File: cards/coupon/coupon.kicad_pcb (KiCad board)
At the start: 2 copper layers, 100 x 100 mm, 65 parts, among them J1 IN N1 N2 N3, J2 BUS, Q1 2N7000, Q10 2N7000, Q11 2N7000, Q12 2N7000, Q13 2N7000, Q14 2N7000, Q15 2N7000, Q16 2N7000, Q17 2N7000, Q18 2N7000, Q19 2N7000, Q2 2N7000, Q20 2N7000, Q21 2N7000, Q22 2N7000, Q23 2N7000, Q24 2N7000, Q25 2N7000, Q26 2N7000, Q3 2N7000, Q4 2N7000, Q5 2N7000, Q6 2N7000, Q7 2N7000, Q8 2N7000, Q9 2N7000

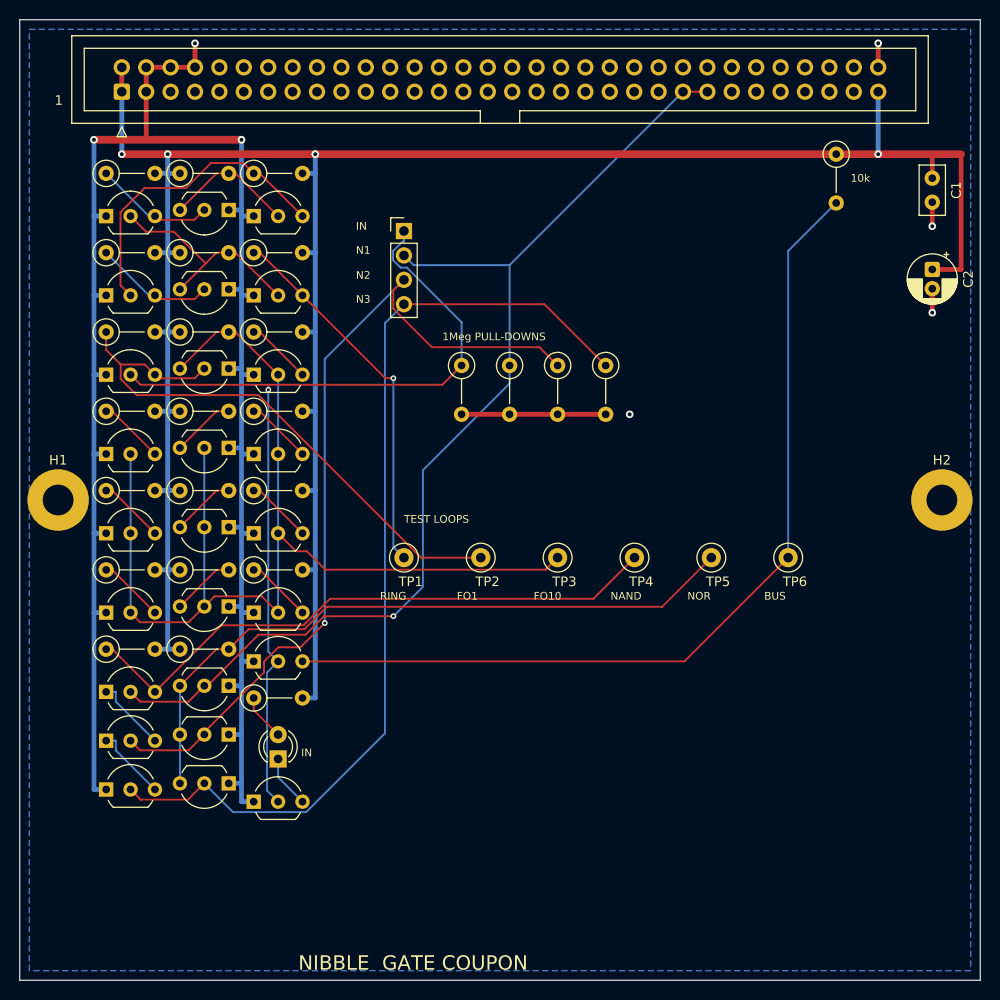
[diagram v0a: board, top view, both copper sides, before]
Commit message: Coupon respun with every cell on it (D056): the bench's expected readings from its own netlist
The coupon is what proves the simulations right before the second order, and
the old one measured only the inverter. It now carries, each with a test
loop: the 5-inverter ring (a buffered loop and a raw one on the ring node),
fan-out 1 and 10, NAND3 and NOR3, the bus driver against 10k, the clock
card's oscillator (its Schmitt pair and 100k + 47 nF, the same parts drawn
on the sheet), a master-slave flip-flop wired as a toggle with the
asynchronous reset the counters and the sequencer use, the D053 line
driver (1k inverter, 100 ohm, diode, 10k pull-down; 3.3 nF clipped on at
the bench), a diode-connected transistor on 4.7k that reads its own
threshold, and a program row (3.3k, 1N4148, 220k). Inputs IN N1 N2 N3 RST
on a 6-pin header with 1 Meg pull-downs, power on a 2-pin header for the
bench supply, fifteen loops. 57 transistors on six tile columns of one
100 x 100 card; ERC 0, one freerouting pass, DRC 0 errors (one dangling
trunk end), 0 open under JLCPCB's minimum rules too.

sim/tb_coupon.py simulates the routed card's kicad export (or the gate list
plus the sheet parts, which agree at every uniform corner) at TYP, LO, HI
and MIX seeds 1..3, a x10 probe on every loop, and writes the bands the
bench must land in: sim/results/coupon_expected.md. Ring 5.9 to 23.6 us
(14.6 typical), fan-out-1 rise 10 to 12 us, fan-out-10 rise 67 to 77 us,
stacks under 2 mV, Schmitt hysteresis 0.4 V about the threshold,
oscillator 1.64 to 2.55 ms, Q at half that with one edge per clock edge,
DRV 4.0 V high, 6.6 us up and 49 us down into 3.3 nF, VTO 0.88 to 3.02 V,
ROM 4.52 V, 5 to 8 mA with IN low and 11 to 14 mA with IN high.

Two things the testbench found before the copper did: with low-threshold
transistors the ring swings only to 1.6 to 3 V and a high-threshold buffer
never switches (the buffered loop was blind at two MIX seeds; hence the
raw RING0 loop), and while RST holds the flip-f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
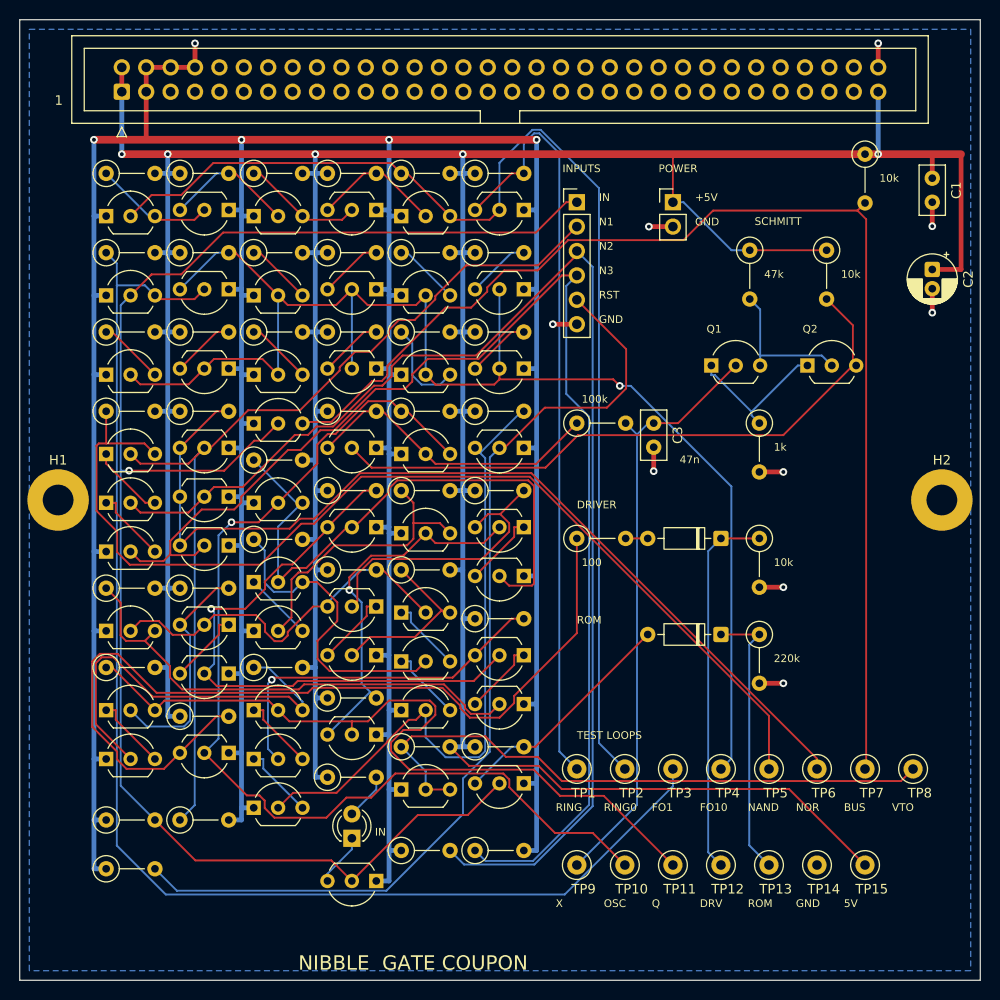
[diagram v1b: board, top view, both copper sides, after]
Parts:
- added C3: 47n, C_Disc_D5.0mm_W2.5mm_P2.50mm, F.Cu at (66.0, 42.0)
- added D2: 1N4148, D_DO-35_SOD27_P7.62mm_Horizontal, F.Cu at (73.0, 54.0)
- added D3: 1N4148, D_DO-35_SOD27_P7.62mm_Horizontal, F.Cu at (73.0, 64.0)
- added J3: BUS, IDC-Header_2x32_P2.54mm_Vertical, F.Cu at (10.6, 7.50)
- added Q27: 2N7000, TO-92_Inline_Wide, F.Cu at (39.7, 45.2)
- added Q28: 2N7000, TO-92_Inline_Wide, F.Cu at (52.5, 44.6)
- added Q29: 2N7000, TO-92_Inline_Wide, F.Cu at (24.4, 50.3)
- added Q30: 2N7000, TO-92_Inline_Wide, F.Cu at (37.1, 52.8)
- added Q31: 2N7000, TO-92_Inline_Wide, F.Cu at (39.7, 53.5)
- added Q32: 2N7000, TO-92_Inline_Wide, F.Cu at (52.5, 52.8)
- added Q33: 2N7000, TO-92_Inline_Wide, F.Cu at (52.5, 57.9)
- added Q34: 2N7000, TO-92_Inline_Wide, F.Cu at (24.4, 58.5)
- added Q35: 2N7000, TO-92_Inline_Wide, F.Cu at (24.4, 63.6)
- added Q36: 2N7000, TO-92_Inline_Wide, F.Cu at (37.1, 61.1)
- added Q37: 2N7000, TO-92_Inline_Wide, F.Cu at (37.1, 66.2)
- added Q38: 2N7000, TO-92_Inline_Wide, F.Cu at (39.7, 61.7)
- added Q39: 2N7000, TO-92_Inline_Wide, F.Cu at (39.7, 66.8)
- added Q40: 2N7000, TO-92_Inline_Wide, F.Cu at (39.7, 71.9)
- added Q41: 2N7000, TO-92_Inline_Wide, F.Cu at (9.00, 63.6)
- added Q42: 2N7000, TO-92_Inline_Wide, F.Cu at (21.8, 63.0)
- added Q43: 2N7000, TO-92_Inline_Wide, F.Cu at (21.8, 68.1)
- added Q44: 2N7000, TO-92_Inline_Wide, F.Cu at (52.5, 66.2)
- added Q45: 2N7000, TO-92_Inline_Wide, F.Cu at (52.5, 71.2)
- added Q46: 2N7000, TO-92_Inline_Wide, F.Cu at (9.00, 71.9)
- added Q47: 2N7000, TO-92_Inline_Wide, F.Cu at (9.00, 77.0)
- added Q48: 2N7000, TO-92_Inline_Wide, F.Cu at (24.4, 71.9)
- added Q49: 2N7000, TO-92_Inline_Wide, F.Cu at (24.4, 77.0)
- added Q50: 2N7000, TO-92_Inline_Wide, F.Cu at (24.4, 82.0)
- added Q51: 2N7000, TO-92_Inline_Wide, F.Cu at (37.1, 74.4)
- added Q52: 2N7000, TO-92_Inline_Wide, F.Cu at (21.8, 76.3)
- added Q53: 2N7000, TO-92_Inline_Wide, F.Cu at (39.7, 80.1)
- added Q54: 2N7000, TO-92_Inline_Wide, F.Cu at (52.5, 79.5)
- added Q55: 2N7000, TO-92_Inline_Wide, F.Cu at (37.1, 89.7)
- added Q56: 2N7000, TO-92_Inline_Wide, F.Cu at (72.0, 36.0)
- added Q57: 2N7000, TO-92_Inline_Wide, F.Cu at (82.0, 36.0)
- added R27: 47k, R_Axial_DIN0207_L6.3mm_D2.5mm_P5.08mm_Vertical, F.Cu at (39.7, 49.0)
- added R28: 47k, R_Axial_DIN0207_L6.3mm_D2.5mm_P5.08mm_Vertical, F.Cu at (47.4, 49.0)
- added R29: 47k, R_Axial_DIN0207_L6.3mm_D2.5mm_P5.08mm_Vertical, F.Cu at (24.4, 54.1)
- added R30: 47k, R_Axial_DIN0207_L6.3mm_D2.5mm_P5.08mm_Vertical, F.Cu at (32.0, 57.3)
- added R31: 47k, R_Axial_DIN0207_L6.3mm_D2.5mm_P5.08mm_Vertical, F.Cu at (39.7, 57.3)
- added R32: 47k, R_Axial_DIN0207_L6.3mm_D2.5mm_P5.08mm_Vertical, F.Cu at (9.00, 59.2)
- added R33: 47k, R_Axial_DIN0207_L6.3mm_D2.5mm_P5.08mm_Vertical, F.Cu at (16.7, 59.2)
- added R34: 47k, R_Axial_DIN0207_L6.3mm_D2.5mm_P5.08mm_Vertical, F.Cu at (47.4, 62.4)
- added R35: 47k, R_Axial_DIN0207_L6.3mm_D2.5mm_P5.08mm_Vertical, F.Cu at (9.00, 67.4)
- added R36: 47k, R_Axial_DIN0207_L6.3mm_D2.5mm_P5.08mm_Vertical, F.Cu at (24.4, 67.4)
- added R37: 47k, R_Axial_DIN0207_L6.3mm_D2.5mm_P5.08mm_Vertical, F.Cu at (32.0, 70.6)
- added R38: 1k, R_Axial_DIN0207_L6.3mm_D2.5mm_P5.08mm_Vertical, F.Cu at (16.7, 72.5)
- added R39: 4.7k, R_Axial_DIN0207_L6.3mm_D2.5mm_P5.08mm_Vertical, F.Cu at (39.7, 75.7)
- added R40: 3.3k, R_Axial_DIN0207_L6.3mm_D2.5mm_P5.08mm_Vertical, F.Cu at (47.4, 75.7)
- added R41: 1k, R_Axial_DIN0207_L6.3mm_D2.5mm_P5.08mm_Vertical, F.Cu at (32.0, 78.9)
- added R42: 1Meg, R_Axial_DIN0207_L6.3mm_D2.5mm_P5.08mm_Vertical, F.Cu at (9.00, 83.3)
- added R43: 1Meg, R_Axial_DIN0207_L6.3mm_D2.5mm_P5.08mm_Vertical, F.Cu at (16.7, 83.3)
- added R44: 1Meg, R_Axial_DIN0207_L6.3mm_D2.5mm_P5.08mm_Vertical, F.Cu at (39.7, 86.5)
- added R45: 1Meg, R_Axial_DIN0207_L6.3mm_D2.5mm_P5.08mm_Vertical, F.Cu at (47.4, 86.5)
- added R46: 1Meg, R_Axial_DIN0207_L6.3mm_D2.5mm_P5.08mm_Vertical, F.Cu at (9.00, 88.4)
- added R47: 47k, R_Axial_DIN0207_L6.3mm_D2.5mm_P5.08mm_Vertical, F.Cu at (76.0, 24.0)
- added R48: 10k, R_Axial_DIN0207_L6.3mm_D2.5mm_P5.08mm_Vertical, F.Cu at (84.0, 24.0)
- added R49: 1k, R_Axial_DIN0207_L6.3mm_D2.5mm_P5.08mm_Vertical, F.Cu at (77.0, 42.0)
- added R50: 100k, R_Axial_DIN0207_L6.3mm_D2.5mm_P5.08mm_Vertical, F.Cu at (58.0, 42.0)
- added R51: 100, R_Axial_DIN0207_L6.3mm_D2.5mm_P5.08mm_Vertical, F.Cu at (58.0, 54.0)
- added R52: 10k, R_Axial_DIN0207_L6.3mm_D2.5mm_P5.08mm_Vertical, F.Cu at (77.0, 54.0)
- added R53: 220k, R_Axial_DIN0207_L6.3mm_D2.5mm_P5.08mm_Vertical, F.Cu at (77.0, 64.0)
- added TP10: TP_OSC, TestPoint_Loop_D2.50mm_Drill1.0mm, F.Cu at (63.0, 88.0)
- added TP11: TP_Q, TestPoint_Loop_D2.50mm_Drill1.0mm, F.Cu at (68.0, 88.0)
- added TP12: TP_DRV, TestPoint_Loop_D2.50mm_Drill1.0mm, F.Cu at (73.0, 88.0)
- added TP13: TP_ROM, TestPoint_Loop_D2.50mm_Drill1.0mm, F.Cu at (78.0, 88.0)
- added TP14: GND, TestPoint_Loop_D2.50mm_Drill1.0mm, F.Cu at (83.0, 88.0)
- added TP15: +5V, TestPoint_Loop_D2.50mm_Drill1.0mm, F.Cu at (88.0, 88.0)
- added TP7: TP_BUS, TestPoint_Loop_D2.50mm_Drill1.0mm, F.Cu at (88.0, 78.0)
- added TP8: TP_VTO, TestPoint_Loop_D2.50mm_Drill1.0mm, F.Cu at (93.0, 78.0)
- added TP9: X, TestPoint_Loop_D2.50mm_Drill1.0mm, F.Cu at (58.0, 88.0)
- J1: value IN N1 N2 N3 -> IN N1 N2 N3 RST GND; footprint PinHeader_1x04_P2.54mm_Vertical -> PinHeader_1x06_P2.54mm_Vertical
- J2: value BUS -> +5V GND; footprint IDC-Header_2x32_P2.54mm_Vertical -> PinHeader_1x02_P2.54mm_Vertical
- R1: value 1Meg -> 10k
- R2, R3, R4: value 1Meg -> 47k
- R22: value 47k -> 4.7k
- R26: value 1k -> 47k
- R5: value 10k -> 47k
- TP2: value TP_FO1 -> RING0
- TP3: value TP_FO10 -> TP_FO1
- TP4: value TP_NAND -> TP_FO10
- TP5: value TP_NOR -> TP_NAND
- TP6: value TP_BUS -> TP_NOR
- moved J2 58.5 mm to (68.0, 19.0), turned to 0 degrees
- moved R5 53.0 mm to (32.0, 16.0), turned to 0 degrees
- moved R1 47.4 mm to (88.0, 14.0)
- moved R2 46.5 mm to (9.00, 16.0), turned to 0 degrees
- moved R24 45.7 mm to (47.4, 40.8)
- moved R3 44.1 mm to (16.7, 16.0), turned to 0 degrees
- moved R4 41.7 mm to (24.4, 16.0), turned to 0 degrees
- moved Q26 39.0 mm to (37.1, 44.6), turned to 180 degrees
- moved Q16 37.9 mm to (37.1, 36.3), turned to 180 degrees
- moved Q18 37.9 mm to (52.5, 36.3), turned to 180 degrees
- moved R18 34.9 mm to (39.7, 32.5)
- moved R19 34.9 mm to (47.4, 32.5)
- moved Q10 32.9 mm to (37.1, 28.1), turned to 180 degrees
- moved Q12 32.9 mm to (52.5, 28.1), turned to 180 degrees
- moved R12 31.8 mm to (39.7, 24.3)
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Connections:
- J2 pad 2: +5V -> GND
- Q26 pad 2: IN -> VD2
- Q26 pad 3: Net-(D1-K) -> SA
- R1 pad 1: IN -> +5V
- R1 pad 2: GND -> TP_BUS
- R10 pad 1: +5V -> LOAD0
- R10 pad 2: RING0 -> +5V
- R11 pad 1: TP_RING -> +5V
- R11 pad 2: +5V -> LOAD1
- R12 pad 1: TP_FO1 -> LOAD2
- R13 pad 2: TP_FO10 -> LOAD3
- R14 pad 1: LOAD0 -> LOAD4
- R15 pad 1: LOAD1 -> +5V
- R15 pad 2: +5V -> LOAD5
- R16 pad 1: +5V -> LOAD6
- R16 pad 2: LOAD2 -> +5V
- R17 pad 1: LOAD3 -> +5V
- R17 pad 2: +5V -> LOAD7
- R18 pad 1: LOAD4 -> LOAD8
- R19 pad 2: LOAD5 -> LOAD9
- R2 pad 1: N1 -> RING1
- R2 pad 2: GND -> +5V
- R20 pad 1: LOAD6 -> TP_NAND
- R21 pad 1: LOAD7 -> +5V
- R21 pad 2: +5V -> TP_NOR
- R22 pad 2: LOAD8 -> SA
- R23 pad 1: LOAD9 -> TP_OSC
- R24 pad 1: TP_NAND -> +5V
- R24 pad 2: +5V -> RSTN
- R25 pad 1: +5V -> TP_Q_ckn
- R25 pad 2: TP_NOR -> +5V
- R26 pad 1: Net-(D1-A) -> +5V
- R26 pad 2: +5V -> TP_Q_ckb
- R3 pad 1: N2 -> +5V
- R3 pad 2: GND -> RING2
- R4 pad 1: N3 -> RING3
- R4 pad 2: GND -> +5V
- R5 pad 2: TP_BUS -> RING4
- R6 pad 1: RING1 -> RING0
- R7 pad 2: RING2 -> TP_RING
- R8 pad 1: RING3 -> TP_FO1
- R9 pad 1: RING4 -> +5V
- R9 pad 2: +5V -> TP_FO10
- TP2 pad 1: TP_FO1 -> RING0
- TP3 pad 1: TP_FO10 -> TP_FO1
- TP4 pad 1: TP_NAND -> TP_FO10
- TP5 pad 1: TP_NOR -> TP_NAND
- TP6 pad 1: TP_BUS -> TP_NOR
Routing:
- net GND: track 220.5 -> 444.0 mm, vias 7 -> 14
- net +5V: track 256.1 -> 428.9 mm, vias 4 -> 5
- net TP_OSC: track 0.00 -> 109.9 mm, vias 0 -> 1
- net RST: track 0.00 -> 103.1 mm
- net RING0: track 23.5 -> 124.3 mm
- net DRVN: track 0.00 -> 93.6 mm
- net TP_Q: track 0.00 -> 81.8 mm
- net TP_FO1: track 60.4 -> 138.8 mm
- net IN: track 98.4 -> 168.1 mm
- net RSTN: track 0.00 -> 68.1 mm
- net VD2: track 0.00 -> 65.8 mm
- net TP_VTO: track 0.00 -> 64.2 mm
- net TP_Q_ckb: track 0.00 -> 62.8 mm, vias 0 -> 1
- net X: track 0.00 -> 62.3 mm
- net TP_Q_ckn: track 0.00 -> 61.8 mm
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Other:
- board text added: "+5V"
- board text added: "100"
- board text added: "100k"
- board text added: "1k"
- board text added: "220k"
- board text added: "47k"
- board text added: "47n"
- board text added: "5V"
- board text added: "DRIVER"
- board text added: "DRV"
- board text added: "GND"
- board text added: "INPUTS"
- board text added: "OSC"
- board text added: "POWER"
- board text added: "Q"
- board text added: "Q1"
- board text added: "Q2"
- board text added: "RING0"
- board text added: "ROM"
- board text added: "RST"
- board text added: "SCHMITT"
- board text added: "VTO"
- board text added: "X"
- board text removed: "1Meg PULL-DOWNS"

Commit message: The bus headers go on the back of all 26 boards, no track moved; the silkscreen refitted (D059, D062)
An IDC socket lies across its ribbon, so the ribbon could never run along a
row of cards as drawn. It runs behind them, and the 64-pin headers are
soldered on the back. This commit is that move, made in place on the routed
boards: no board was routed again.

How the header sits (D062): in the holes it had, turned over top to bottom,
notch toward the top edge. A pin of the odd row is then in the hole its even
neighbour had, so the two signals of every pair of pins change places: CLK
is pin 6, RST pin 8, +5V pins 1, 2 and 64. bus.py keeps both tables: PINS,
what the header's pins carry, and HOLES, what the copper was routed to.

The proof, on all 26 boards against 992a90f (sim/board_diff.py):
  netlist the same, element for element; every track, every via and every
  hole the same; each copper and mask layer differs by two pad shapes per
  header (pin 1's square went to the hole beside it, both on +5V) and the
  ground pour's outline round those two pads, nowhere else by more than a
  tenth of a micrometre.
sim/rebuild_check.py runs every builder into a scratch directory: each
writes the plan and the netlist that are committed, so a rebuild gives
this board. order_check.py --machine holds every pad of the 27 headers to
bus.py and requires them on the back.

What the move costs: on the ribbon RST had a ground conductor on both
sides; now one neighbour is BUS1#. tb_rst_neighbour.py puts the two lines
on the bench with every gate the routed boards hang on them: RST rises
0.28 to 0.43 V when BUS1# is released, against a lowest threshold of 0.8 V
(sim/results/rst_neighbour.md). The machine deck's crosstalk option now
couples the pins that are neighbours on the ribbon; the crosstalk stage of
the machine gate has to be run again on that order.

Silkscreen (pcb.fit_silk): every label to 1.0 mm where it has room, off
pads, vias, outlines and other labels, out from under the pa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
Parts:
- J3: moved to B.Cu
- moved J3 2.54 mm to (10.6, 4.96), turned to -90 degrees
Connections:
- J3 pad 5: unconnected-(J3-Pin_5-Pad5) -> GND
- J3 pad 6: GND -> unconnected-(J3-Pin_6-Pad6)
- J3 pad 63: +5V -> GND
- J3 pad 64: GND -> +5V
- J3 pad 7: unconnected-(J3-Pin_7-Pad7) -> GND
- J3 pad 8: GND -> unconnected-(J3-Pin_8-Pad8)
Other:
- board text added: "2"
- board text added: "63"
- board text added: "64"
- board text added: "HEADER HERE"
- board text added: "HEADER ON THE BACK"
- board text added: "NOTCH TO TOP"

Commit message: Silk: the front no longer says HEADER ON THE BACK; the back says HEADER HERE, which is enough
A "not here" note under the holes on every board, the kind of text that
narrates instead of naming. The back carries the header's outline with
HEADER HERE and NOTCH TO TOP; the front keeps the pin numbers 1, 2, 63,
64. All 26 boards re-silked in place from their plans (no re-route, the
schematics untouched); the order gate's silk rule now wants HEADER HERE
on the back and no HEADER ON THE BACK anywhere. Gate all pass, every
builder writes what is committed, parts tables unchanged.

Co-Authored-By: Claude Fable 5.1 <noreply@anthropic.com>
Claude-Session: https://claude.ai/code/session_01RktbhdQjDu7SpFpvkevyUU
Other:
- board text removed: "HEADER ON THE BACK"
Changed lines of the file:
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@@
-		)
-	)
-	(gr_text "HEADER ON THE BACK"
-		(at 26.63 11.4 0)
-		(layer "F.SilkS")
-		(effects
-			(font
-				(size 1 1)
-				(thickness 0.15)
-			)
-			(justify left)
 		)
 	)

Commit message: The Nibble logo on the front silkscreen of every board
lib/logo/nibble.png traced by sim/logo.py (potracer) into two silkscreen
footprints, lib/nibble.pretty/Logo_Nibble (icon and word, 27 x 8 mm) and
Logo_Nibble_Icon (8 x 8): filled polygons, holes slit in. At 8 mm the
ribbon's lines print 0.39 mm wide and 0.24 mm apart; the fab's minimum
is 0.15. No pads, no copper, out of the parts list and the position file.

pcb.py places it on every board before the labels are fitted
(place_logo): icon and word where a patch 27 x 8 mm is free of pads,
vias, outlines, courtyards, the labels and 1 mm of edge, the icon alone
otherwise, the nearest such patch to the board's name; the fitter then
keeps the labels off it. 25 boards took the full logo, the coupon the
icon. All 26 re-silked in place (no re-route, the schematics untouched).
The order gate wants exactly one logo on a board; bom.py counts it as no
part. Two pcbnew quirks met on the way: a footprint removed in the
fitter's process makes the next loaded board untyped (every hidden
reference became an obstacle and BUS0 on the hub fell back to 0.8 mm),
and after a text is removed the footprints are untyped too, so resilk
takes the old logo off before the texts.

Gate all pass on all 26, every builder writes what is committed, parts
tables unchanged. The pilot's three zips are new again (order-1.md).

Co-Authored-By: Claude Fable 5.1 <noreply@anthropic.com>
Claude-Session: https://claude.ai/code/session_01RktbhdQjDu7SpFpvkevyUU
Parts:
- added LOGO: Logo_Nibble_Icon, Logo_Nibble_Icon, F.Cu at (25.5, 90.9)

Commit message: The logo on the sequencer alone: one maker's mark, not a product line
With the logo on all 26 the machine looked factory-made. It stays on the
sequencer, the big board in the middle that people look at; the cards
carry their name. A board gets the logo when its plan says extra.logo
(the sequencer's builder does), none otherwise, and the order gate holds
each board to its plan. The 25 cards re-silked in place (no re-route).
Gate all pass, builders write what is committed, parts tables unchanged.
The pilot's three zips are new again (order-1.md).

Co-Authored-By: Claude Fable 5.1 <noreply@anthropic.com>
Claude-Session: https://claude.ai/code/session_01RktbhdQjDu7SpFpvkevyUU
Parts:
- removed LOGO: Logo_Nibble_Icon, Logo_Nibble_Icon
